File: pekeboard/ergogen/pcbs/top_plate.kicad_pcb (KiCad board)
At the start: 2 copper layers, 150.9 x 124.7 mm, 0 parts

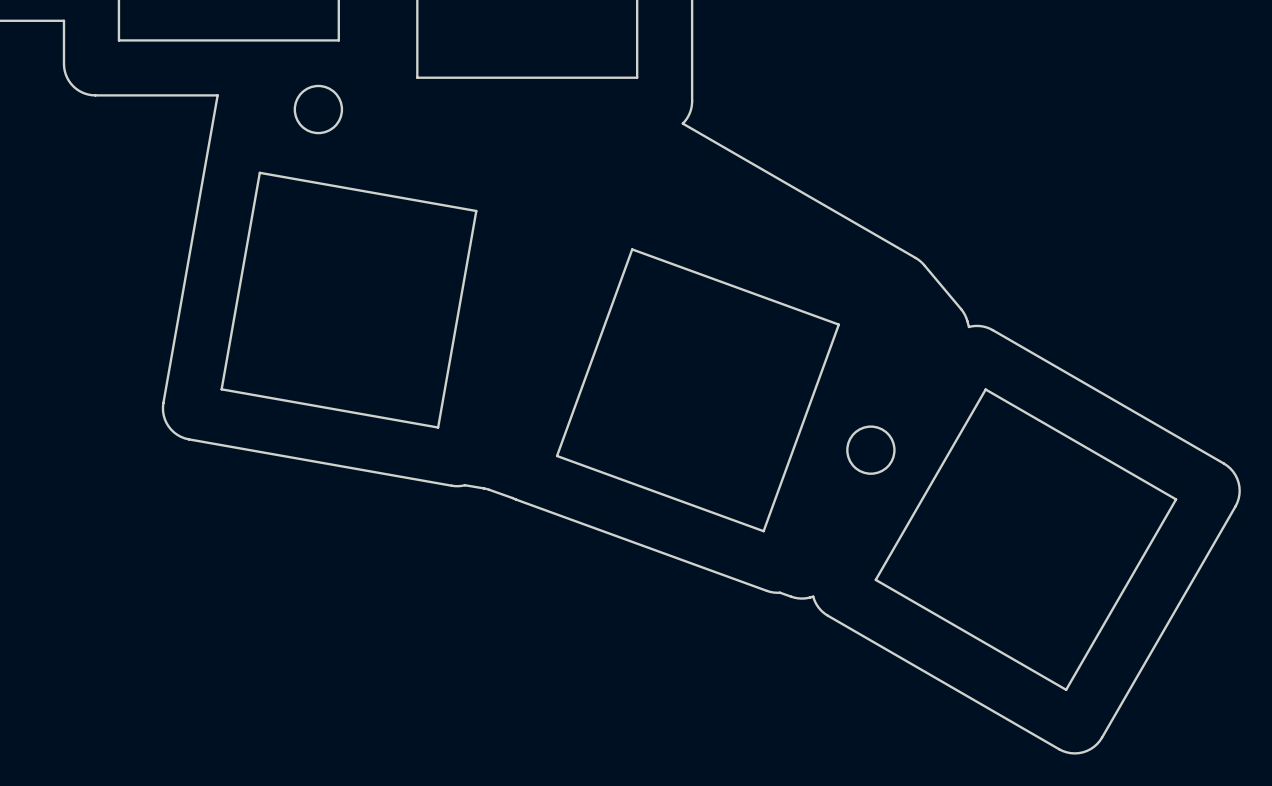
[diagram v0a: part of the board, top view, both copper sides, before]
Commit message: Less spread for thumb cluster
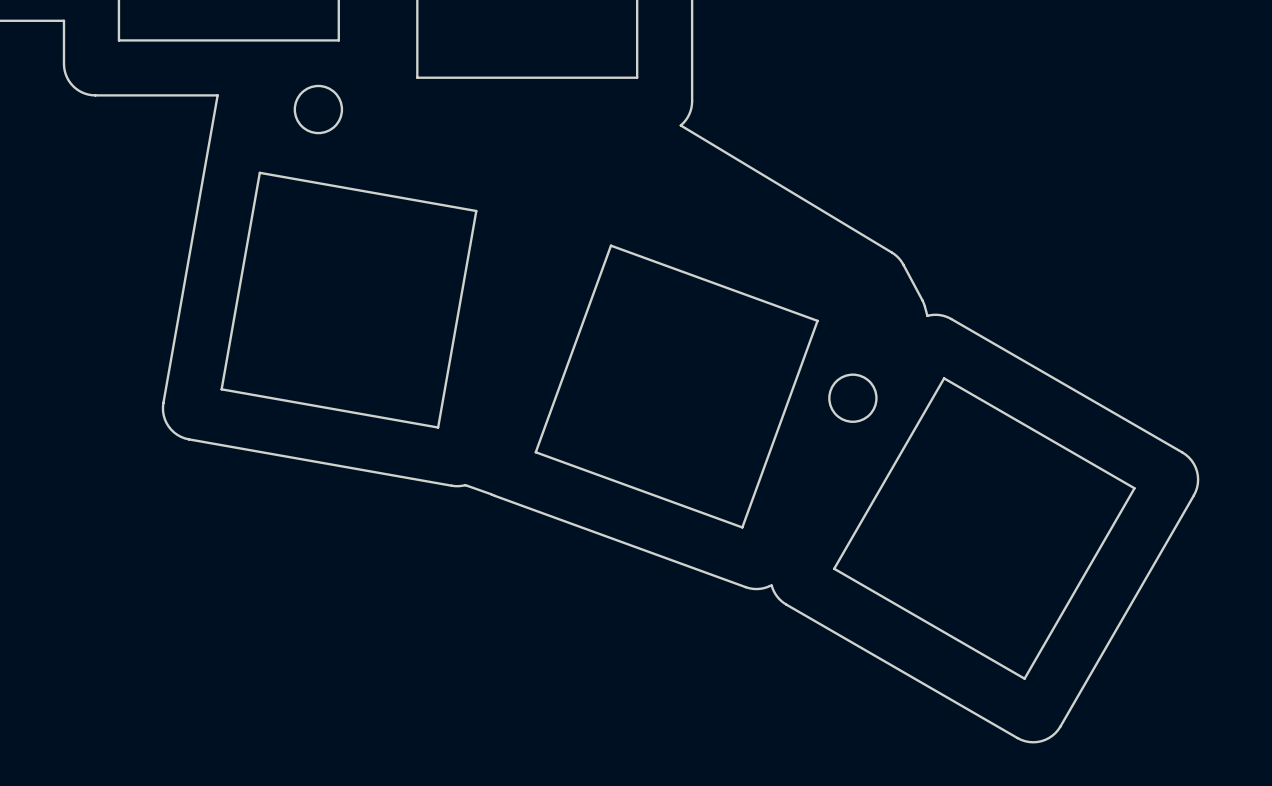
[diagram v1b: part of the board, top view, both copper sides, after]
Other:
- board size 150.9 x 124.7 mm -> 148.2 x 123.9 mm
